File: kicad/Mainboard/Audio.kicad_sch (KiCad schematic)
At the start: 76 parts, among them J10 MIC_EXT, J12 SPK_EXT, Q4 BSS138, Q5 BSS138, SW1 INT_PTT_SW, U10 LM386, U8 HEF4066B, U9 OPA340UA

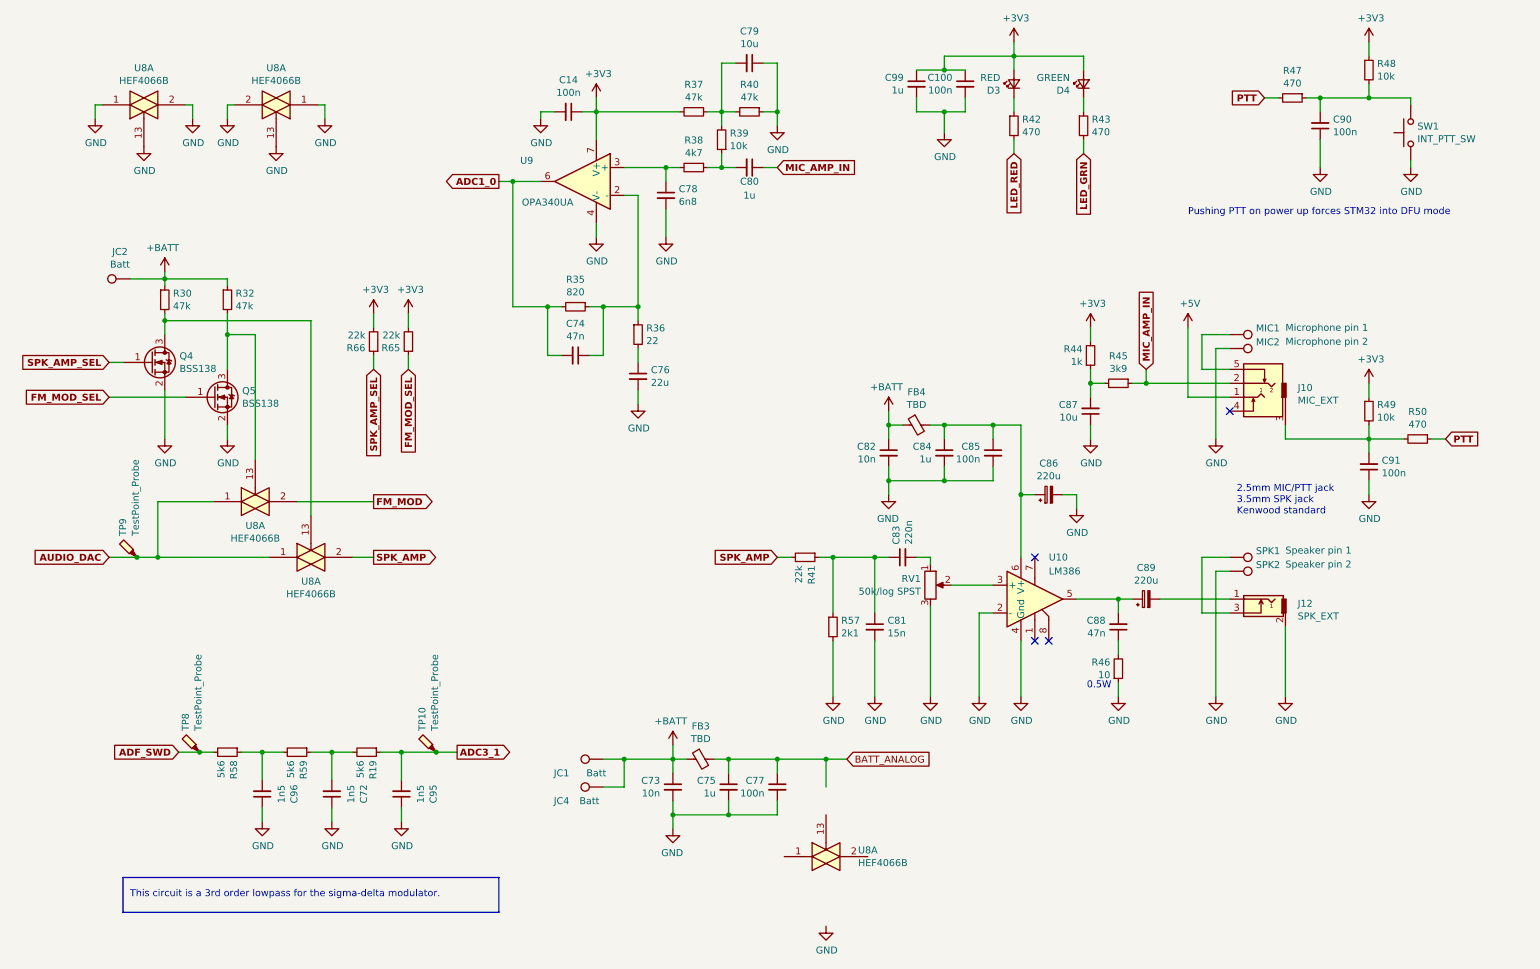
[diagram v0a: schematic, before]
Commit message: Add C106 in parallel to R21
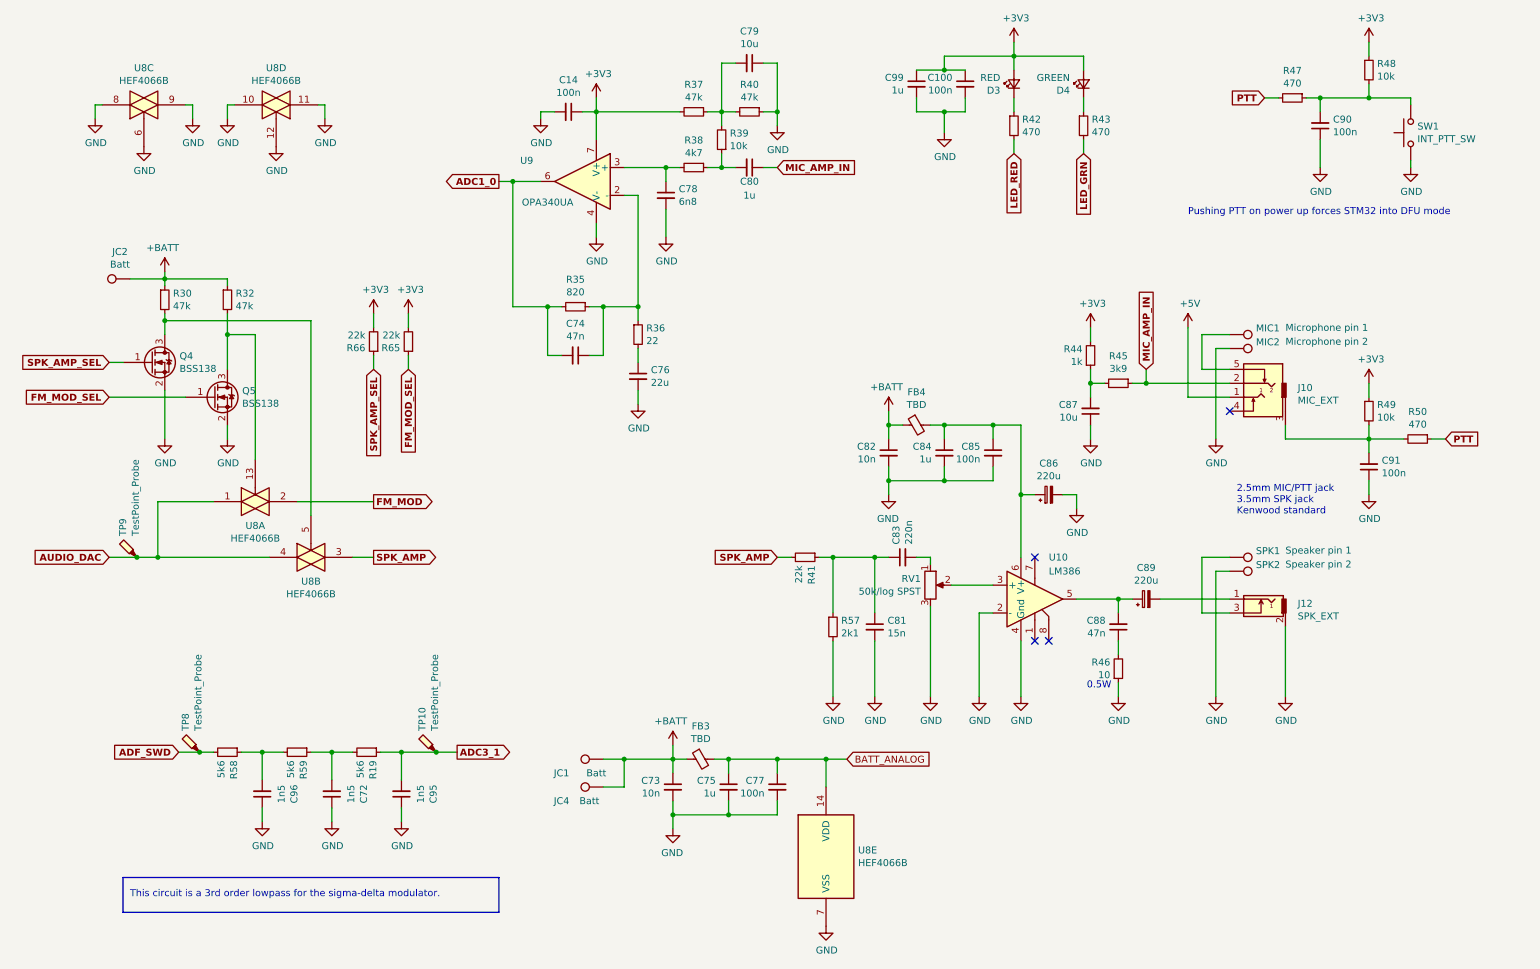
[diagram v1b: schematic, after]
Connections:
- net AUDIO_DAC: now also U8.4; no longer U8.1
- net BATT_ANALOG: now also U8.14 (VDD)
- net GND: now also U8.10, U8.11, U8.12, U8.6, U8.7 (VSS), U8.8, U8.9; no longer U8.1, U8.1, U8.13, U8.13, U8.2, U8.2
- net SPK_AMP: now also U8.3; no longer U8.2
- net at Q4.3 (D), R30.2: now also U8.5; no longer U8.13
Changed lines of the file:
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@@
     (pin "2")
   )
-  (symbol (lib_id "Mainboard-rescue:4066-4xxx") (at 66.04 119.38 0) (unit 1)
+  (symbol (lib_id "Mainboard-rescue:4066-4xxx") (at 66.04 119.38 0) (unit 2)
     (in_bom yes) (on_board yes)
     (property "Reference" "U8" (id 0) (at 66.04 123.7742 0))
@@
       (effects (font (size 1.27 1.27)) hide)
     )
-    (pin "1")
-    (pin "13")
-    (pin "2")
+    (pin "3")
+    (pin "4")
+    (pin "5")
   )
-  (symbol (lib_id "Mainboard-rescue:4066-4xxx") (at 160.02 173.99 0) (unit 1)
+  (symbol (lib_id "Mainboard-rescue:4066-4xxx") (at 160.02 173.99 0) (unit 5)
     (in_bom yes) (on_board yes)
     (property "Reference" "U8" (id 0) (at 165.862 172.8216 0)
@@
       (effects (font (size 1.27 1.27)) hide)
     )
-    (pin "1")
-    (pin "13")
-    (pin "2")
+    (pin "14")
+    (pin "7")
   )
-  (symbol (lib_id "Mainboard-rescue:4066-4xxx") (at 35.56 36.83 0) (mirror x) (unit 1)
+  (symbol (lib_id "Mainboard-rescue:4066-4xxx") (at 35.56 36.83 0) (mirror x) (unit 3)
     (in_bom yes) (on_board yes)
     (property "Reference" "U8" (id 0) (at 35.56 30.099 0))
@@
       (effects (font (size 1.27 1.27)) hide)
     )
-    (pin "1")
-    (pin "13")
-    (pin "2")
+    (pin "6")
+    (pin "8")
+    (pin "9")
   )
-  (symbol (lib_id "Mainboard-rescue:4066-4xxx") (at 59.69 36.83 180) (unit 1)
+  (symbol (lib_id "Mainboard-rescue:4066-4xxx") (at 59.69 36.83 180) (unit 4)
     (in_bom yes) (on_board yes)
     (property "Reference" "U8" (id 0) (at 59.69 30.099 0))
@@
       (effects (font (size 1.27 1.27)) hide)
     )
-    (pin "1")
-    (pin "13")
-    (pin "2")
+    (pin "10")
+    (pin "11")
+    (pin "12")
   )
   (symbol (lib_id "Mainboard-rescue:R_Small-device") (at 63.5 154.94 270) (unit 1)
